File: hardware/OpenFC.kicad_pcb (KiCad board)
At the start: 6 copper layers, 37.5 x 37.5 mm, 174 parts, among them J1 5V, J10 5V, J11 5V, J12 5V, J13 5V, J14 5V, J15 5V, J16 5V, J17 5V, J18 5V, J19 5V, J2 5V, J20 5V, J21 5V, J22 5V, J23 5V, J24 5V, J25 5V, J26 5V, J27 5V, J28 5V, J29 5V, J3 5V, J30 5V, J31 5V, J32 5V, J33 5V, J34 5V, J35 5V, J36 5V, J37 5V, J38 5V, J39 5V, J4 5V, J40 5V, J41 5V, J42 5V, J43 5V, J44 5V, J45 5V, J46 5V, J47 5V, J48 5V, J49 5V, J5 5V, J50 5V, J52 5V, J53 5V, J54 5V, J6 5V, J7 5V, J8 5V, J9 5V, P1 SM08B-SRSS-TB(LF)(SN), Q1 DMN1150UFB-7B, Q2 DMN1150UFB-7B, Q3 DMN1150UFB-7B, Q4 DMN1150UFB-7B, U1 TS2306A 240GF MSM 9_C2976675, U18 SN74LVC1G3157DTBR, U19 TLV9061IDPWR, U2 RP2354B_C39843328, U20 TLV3201AIDBVR, U3 LMR51420YFDDCR, U4 LMR51420YFDDCR, U5 TPS2116DRLR, U6 NCV8187AMT180TAG, U7 LP5912-3.3DRVR, U8 SM06B-SRSS-TB(LF)(SN), U9 LSM6DSV16XTR, X1 XTM25012000JT00351001

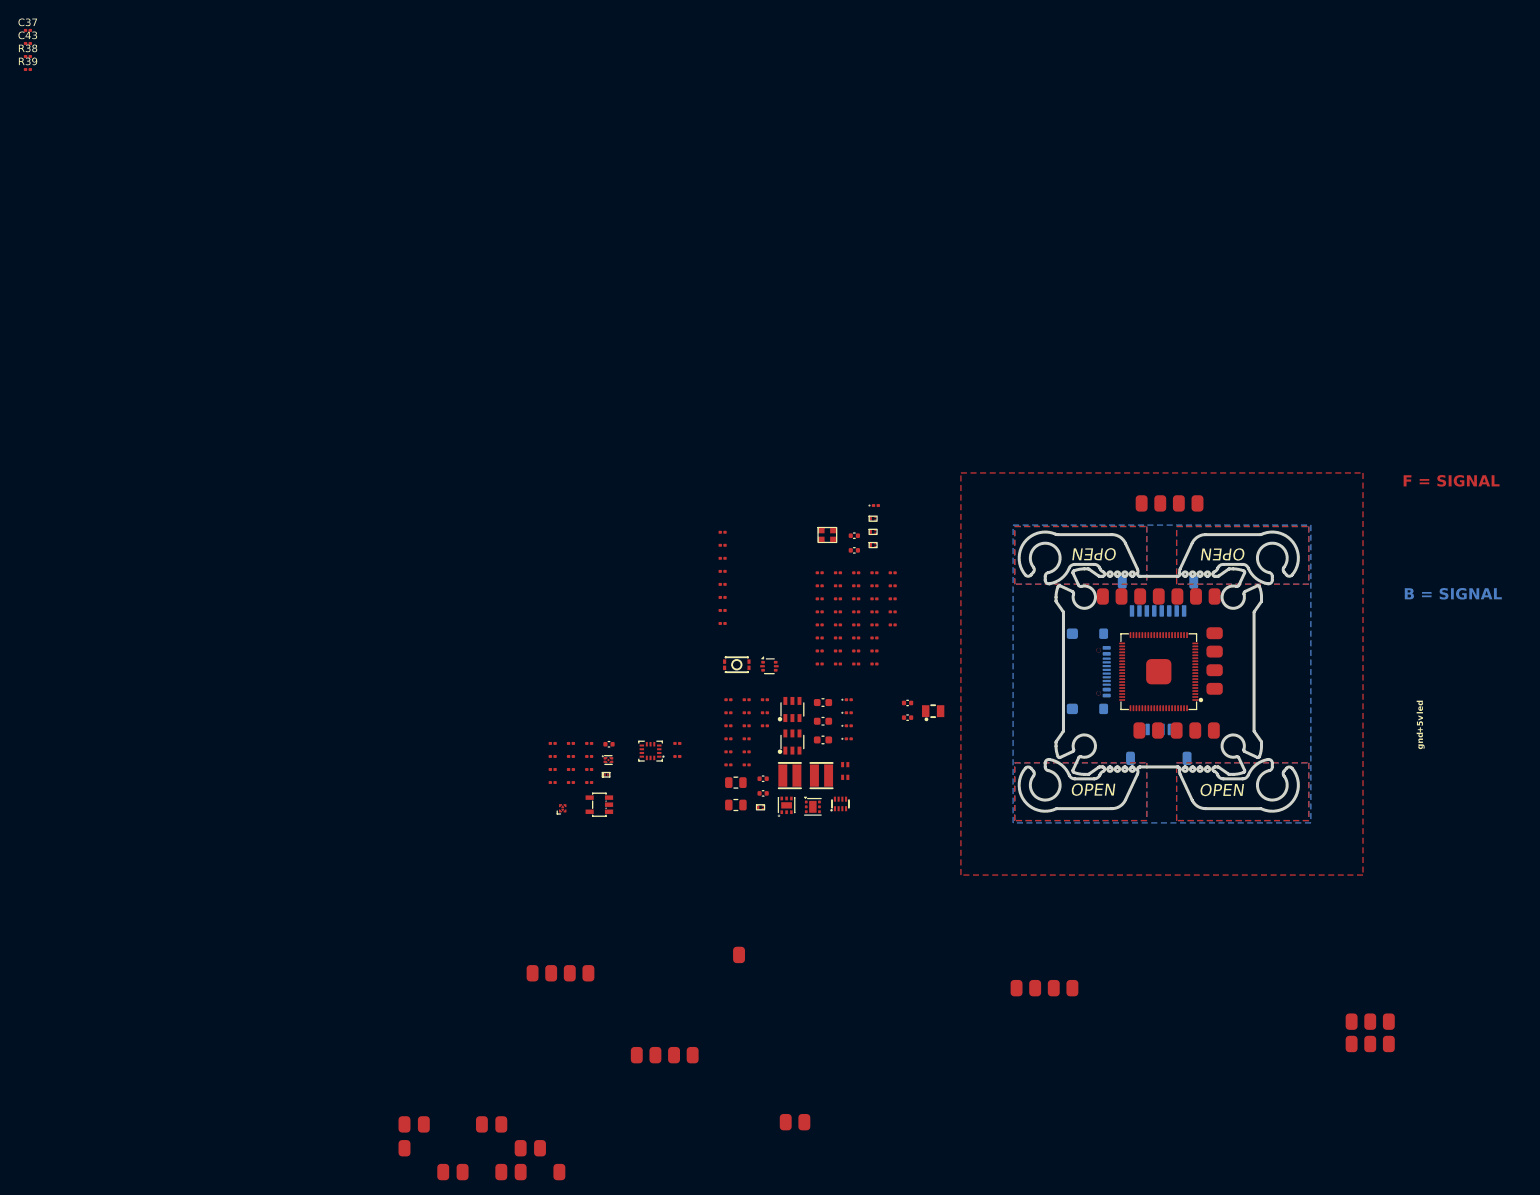
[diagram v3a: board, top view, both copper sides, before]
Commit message: V0.3 routed: pin remap, footprint fixes, EMC checklist, DFM prep
Schematic (user):
- OSD pins remapped to GPIO4-6 (OSD_W/OSD_EN/OSD_SYNC consecutive
  for FB_OSD PIO driver per BF PR#14882)
- SBUS inverter stays on GPIO9 (valid UART1_RX)
- Beeper moved to GPIO36
- Various sub-sheet updates

PCB:
- Full board routed, bottom-side component placement
- Resistor footprints: C_0201 -> R_0201 for correct 3D models
- Capacitor 3D model paths fixed (were pointing to R_0201)
- SD card footprint 3D path fixed (${KIPRJMOD}/lib.3dshapes/)
- 2 footprint 3D paths fixed (SIM, TF-01A: /lib.3dshapes -> ${KIPRJMOD})

Tooling & docs:
- Add EMC checklist (hardware/tools/EMC_CHECKLIST.md)
- Add EMC note script (hardware/tools/add_emc_note.py)
- Update CLAUDE.md: LMR51430 drop-in upgrade noted, connector
  verification, OSD pin mapping

Co-Authored-By: Claude Opus 4.6 (1M context) <noreply@anthropic.com>
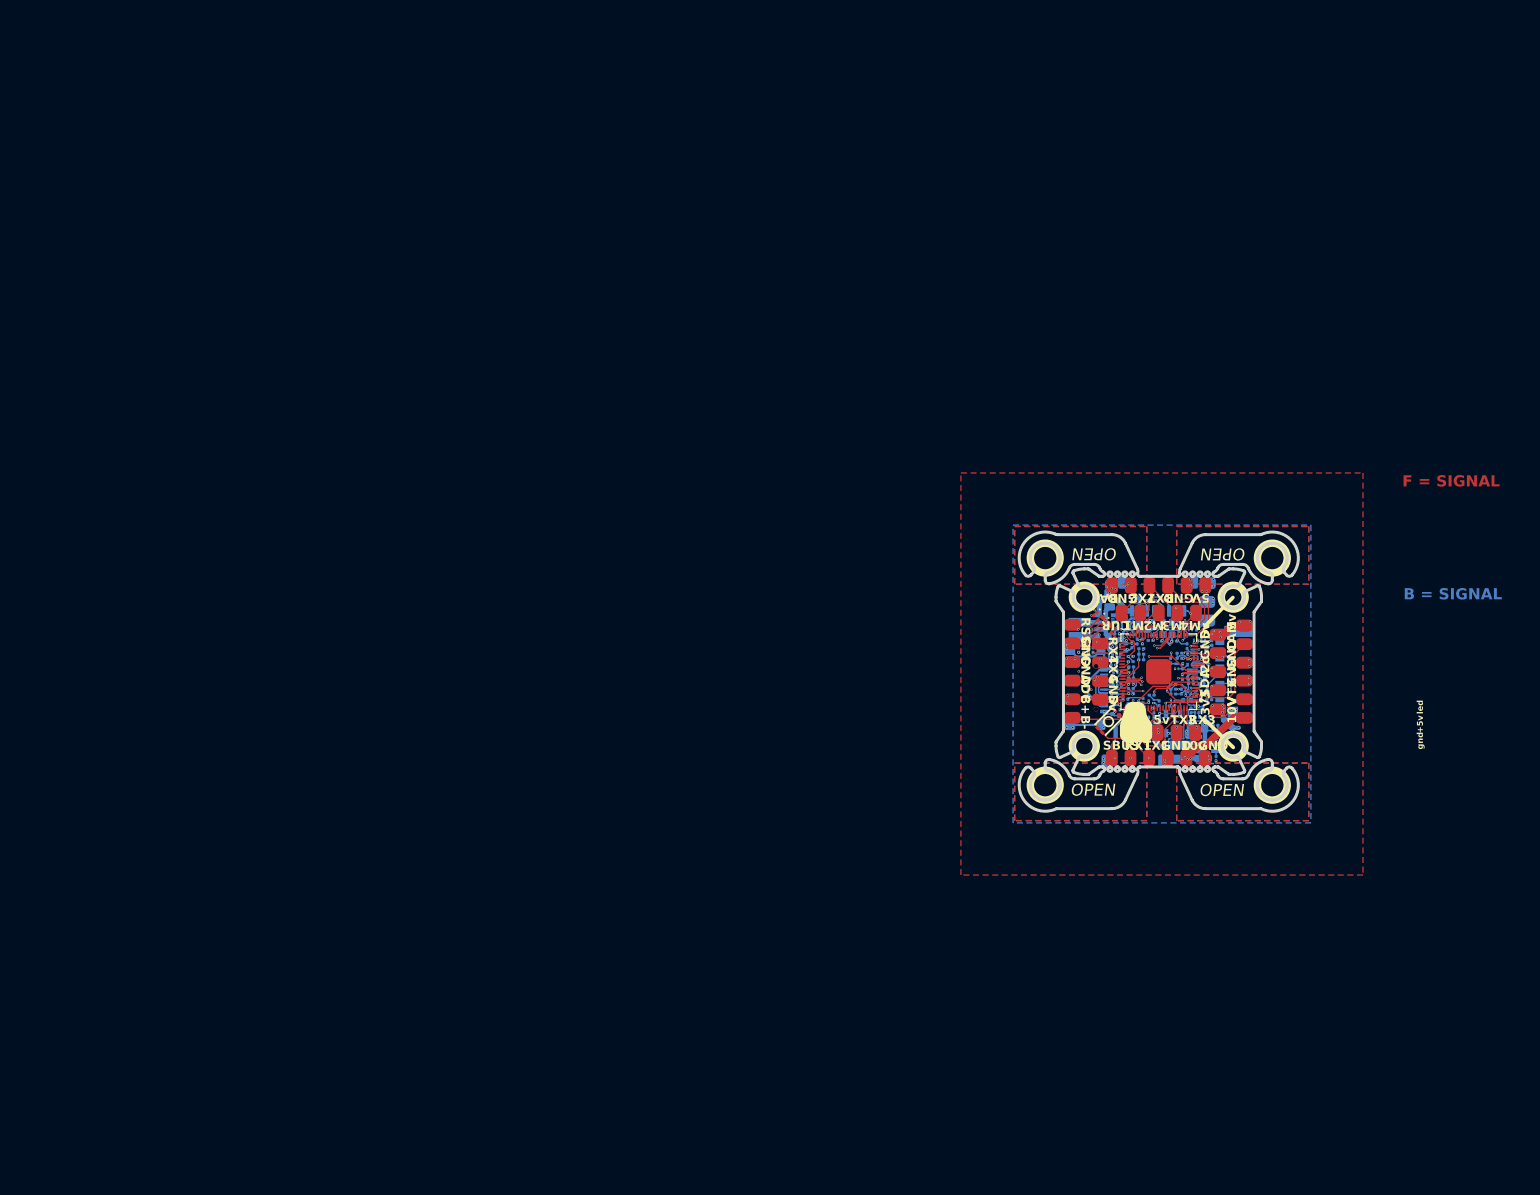
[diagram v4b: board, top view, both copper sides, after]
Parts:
- removed C37: 100n, Capacitor_SMD:C_0201_0603Metric
- removed D8: LED_1_Green, LED_SMD:LED_0201_0603Metric
- removed J16, J17, J19, J20, J23, J24, J3, J6, J9: 5V, lib:small_pad
- removed R37: 200R, Capacitor_SMD:C_0201_0603Metric
- removed R38: 10k, Capacitor_SMD:C_0201_0603Metric
- added Card1: TF-021B-H265, lib:TF-SMD_TF-021B-H265, B.Cu at (162.1, 86.5)
- added D10: LED_1_Green, LED_SMD:LED_0201_0603Metric, F.Cu at (144.1, 78.7)
- added R40: 200R, Resistor_SMD:R_0201_0603Metric, B.Cu at (154.2, 85.0)
- C1, C10, C11, C12, C13, C14, C15, C16, C17, C19, C2, C21, C22, C23, C24, C25, C26, C27, C28, C29, C3, C31, C32, C33, C34, C35, C36, C38, C39, C4, C40, C41, C42, C43, C5, C6, C7, C8, C9, D1, D3, D6, D9, J10, J4, J7, L2, L3, Q1, Q2, Q3, Q4, U18, U19, U20, U3, U4, U5, U6, U7, U9, X1: moved to B.Cu
- C30: value 22uF -> 4.7uF; footprint Capacitor_SMD:C_0603_1608Metric -> Capacitor_SMD:C_0402_1005Metric; moved to B.Cu
- R1, R10, R11, R12, R13, R14, R15, R16, R17, R18, R19, R2, R20, R21, R22, R23, R24, R25, R26, R27, R28, R29, R3, R30, R31, R32, R33, R34, R35, R36, R39, R4, R41, R42, R43, R44, R45, R46, R47, R48, R5, R6, R7, R8, R9: footprint Capacitor_SMD:C_0201_0603Metric -> Resistor_SMD:R_0201_0603Metric; moved to B.Cu
- moved R39 179.8 mm to (159.4, 90.3)
- moved C43 177.5 mm to (154.3, 91.1), turned to 180 degrees
- moved J10 129.0 mm to (159.1, 79.6), turned to 0 degrees
- moved J4 125.9 mm to (159.1, 77.1), turned to 0 degrees
- moved J7 121.5 mm to (159.2, 74.6), turned to 0 degrees
- moved J12 97.9 mm to (151.3, 74.9)
- moved J14 97.9 mm to (156.3, 74.9)
- moved J5 97.9 mm to (158.8, 74.9)
- moved J8 97.9 mm to (153.8, 74.9)
- moved C41 87.7 mm to (158.6, 91.5), turned to -90 degrees
- moved C38 86.9 mm to (158.0, 90.5)
- moved U18 85.5 mm to (156.6, 89.1)
- moved C39 84.9 mm to (155.6, 89.2), turned to 90 degrees
- moved R41 84.5 mm to (158.0, 89.8), turned to 180 degrees
- moved C42 83.6 mm to (154.5, 94.8)
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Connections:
- R15 pad 1: unconnected-(R15-Pad1) -> /IMU/GYRO_CS
- R39 pad 1: unconnected-(R39-Pad1) -> +3.3V
- R39 pad 2: unconnected-(R39-Pad2) -> /BLACKBOX/FLASH_CS
- U2 pad 1: unconnected-(U2-GPIO4-Pad1) -> /OSD/OSD_W
- U2 pad 2: unconnected-(U2-GPIO5-Pad2) -> /OSD/OSD_EN
- U2 pad 3: /RP2350A/BEEPER -> /OSD/OSD_SYNC
- U2 pad 4: unconnected-(U2-GPIO7-Pad4) -> /RP2350A/BEEPER
- U2 pad 42: /OSD/OSD_W -> unconnected-(U2-GPIO33-Pad42)
- U2 pad 43: /OSD/OSD_EN -> unconnected-(U2-GPIO34-Pad43)
- U2 pad 44: /OSD/OSD_SYNC -> unconnected-(U2-GPIO35-Pad44)
- U2 pad 57: /RP2350A/FLASH_CS -> /BLACKBOX/FLASH_CS
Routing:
- net GND: track 0.00 -> 106.8 mm, vias 0 -> 62
- net +3.3V: track 0.00 -> 84.8 mm, vias 0 -> 31
- net +BATT: track 0.00 -> 70.5 mm, vias 0 -> 9
- net +10V: track 0.00 -> 56.2 mm, vias 0 -> 5
- net +1.1V: track 0.00 -> 31.0 mm, vias 0 -> 5
- net +5V: track 0.00 -> 29.9 mm, vias 0 -> 21
- net /BLACKBOX/SPI1.MISO: track 0.00 -> 21.6 mm, vias 0 -> 2
- net /POWER/10V_ENABLE: track 0.00 -> 20.6 mm, vias 0 -> 2
- net /BLACKBOX/FLASH_CS: track 0.00 -> 18.3 mm, vias 0 -> 2
- net /BLACKBOX/SPI1.SCK: track 0.00 -> 16.9 mm, vias 0 -> 2
- net /RP2350A/LED0: track 0.00 -> 16.3 mm, vias 0 -> 2
- net Net-(D10-K): track 0.00 -> 16.0 mm, vias 0 -> 2
- net /BLACKBOX/SPI1.MOSI: track 0.00 -> 15.9 mm, vias 0 -> 2
- net /PADS/RSSI: track 0.00 -> 15.6 mm, vias 0 -> 2
- net +5V_BUCK: track 0.00 -> 14.7 mm, vias 0 -> 2
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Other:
- board text added: "10V"
- board text added: "10v"
- board text added: "3v3"
- board text added: "5V"
- board text added: "5v"
- board text added: "ADC"
- board text added: "B+"
- board text added: "B-"
- board text added: "BAT"
- board text added: "CAM"
- board text added: "CUR"
- board text added: "ECO"
- board text added: "GND"
- board text added: "I2c"
- board text added: "LED"
- board text added: "M1"
- board text added: "M2"
- board text added: "M3"
- board text added: "M4"
- board text added: "RSSI"
- board text added: "RX1"
- board text added: "RX2"
- board text added: "RX3"
- board text added: "RX4"
- board text added: "SBUS"
- board text added: "SDA"
- board text added: "TX1"
- board text added: "TX2"
- board text added: "TX3"
- board text added: "TX4"
- board text added: "VTX"

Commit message: Add V0.3 known issues for V0.4 fix list, update open issues
C28 voltage rating, R30 divider, L2 inductor value, LED0 color,
LMR51430 upgrade path — all noted for next revision. CRIT-5 (ESC
connector) marked fixed. OSD pin mapping updated to GPIO4-6.

Co-Authored-By: Claude Opus 4.6 (1M context) <noreply@anthropic.com>
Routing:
- net +3.3V: track 84.8 -> 87.7 mm
- net /POWER/10V_ENABLE: track 20.6 -> 19.9 mm
- net GND: vias 62 -> 61
